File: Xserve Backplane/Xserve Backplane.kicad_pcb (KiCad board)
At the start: 4 copper layers, 100 x 100 mm, 47 parts, among them CN1 0678008025_SATA_Conn, CN2 0678008025_SATA_Conn, CN3 0678008025_SATA_Conn, J2 Conn_02x03_Odd_Even, J3 1888019-2, J4 SATA_Combo, J5 SATA_Combo, J6 SATA_Combo, Q1 Q_NMOS_DGS, Q2 Q_NMOS_DGS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

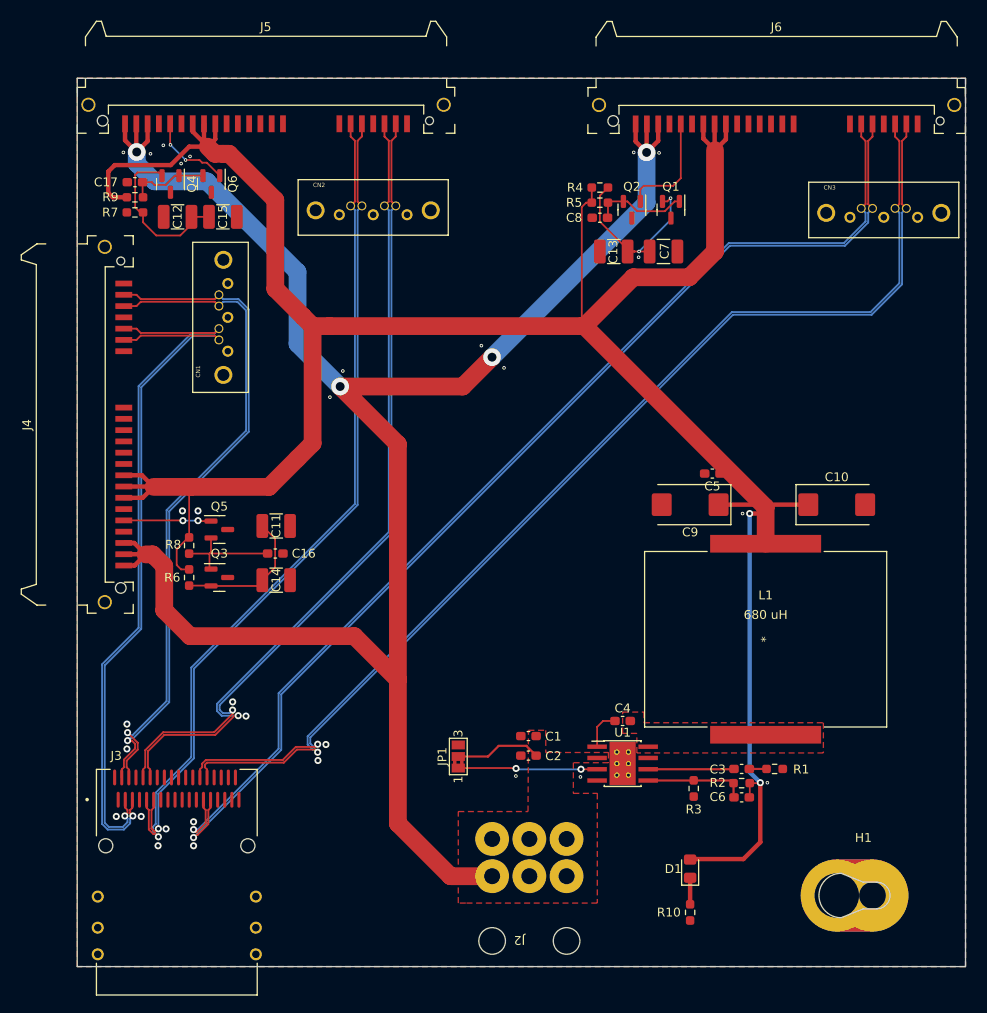
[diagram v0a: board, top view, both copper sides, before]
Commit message: "Ran DRC, changed mosfet footprint"
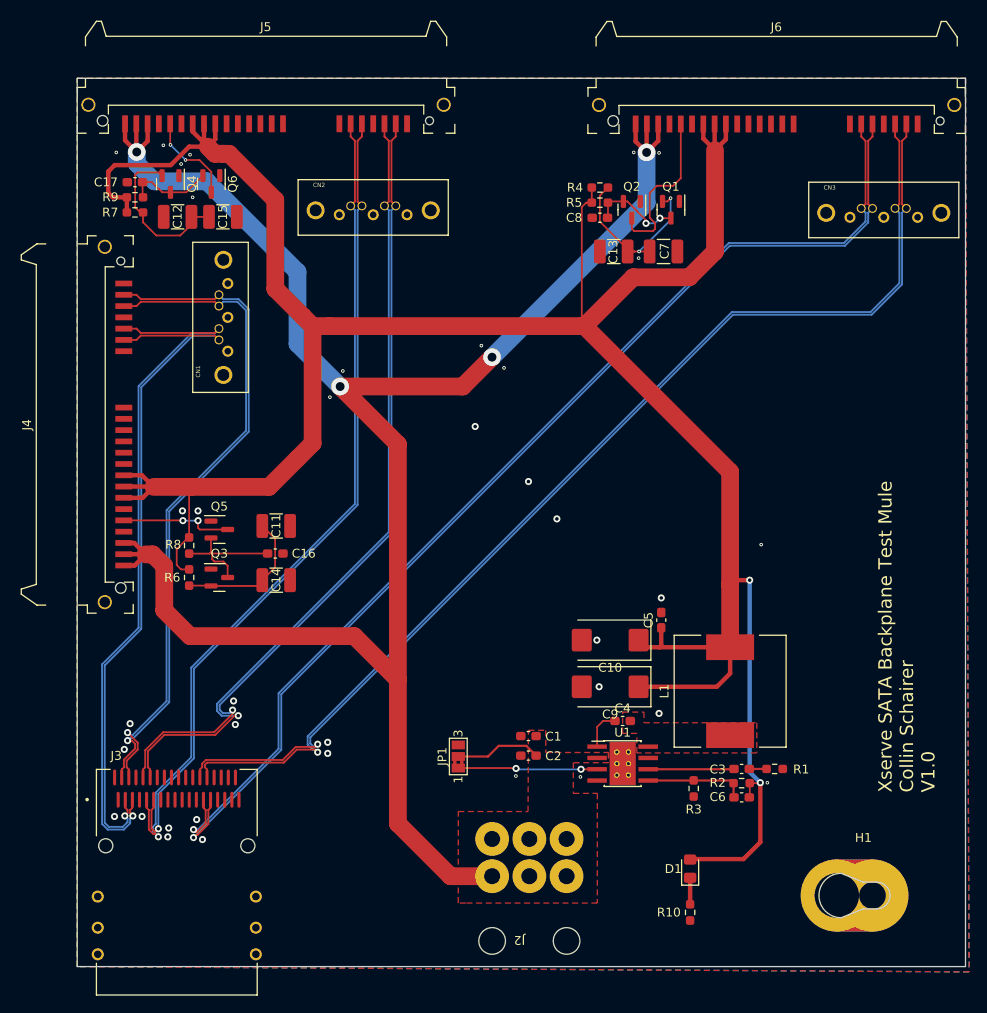
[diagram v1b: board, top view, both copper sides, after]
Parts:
- L1: value 680 uH -> 15 uH; footprint KiCADs:60B474C -> Inductor_SMD:L_12x12mm_H8mm
- moved G*** 71.4 mm to (230.0, 236.2)
- moved C10 29.7 mm to (279.0, 206.2), turned to 180 degrees
- moved C9 22.4 mm to (279.0, 211.5)
- moved C5 17.5 mm to (284.8, 204.0), turned to 90 degrees
- moved L1 7.09 mm to (292.5, 212.0)
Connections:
- C1 pad 2: GND -> Earth
- C10 pad 2: GND -> Earth
- C11 pad 2: GND -> Earth
- C12 pad 2: GND -> Earth
- C13 pad 2: GND -> Earth
- C14 pad 2: GND -> Earth
- C15 pad 2: GND -> Earth
- C16 pad 2: GND -> Earth
- C17 pad 2: GND -> Earth
- C2 pad 2: GND -> Earth
- C5 pad 2: GND -> Earth
- C7 pad 2: GND -> Earth
- C8 pad 2: GND -> Earth
- C9 pad 2: GND -> Earth
- CN1 pad GND1: GND -> Earth
- CN1 pad GND2: GND -> Earth
- CN1 pad GND3: GND -> Earth
- CN1 pad MNT1: GND -> Earth
- CN1 pad MNT2: GND -> Earth
- CN2 pad GND1: GND -> Earth
- CN2 pad GND2: GND -> Earth
- CN2 pad GND3: GND -> Earth
- CN2 pad MNT1: GND -> Earth
- CN2 pad MNT2: GND -> Earth
- CN3 pad GND1: GND -> Earth
- CN3 pad GND2: GND -> Earth
- CN3 pad GND3: GND -> Earth
- CN3 pad MNT1: GND -> Earth
- CN3 pad MNT2: GND -> Earth
- H1 pad 1: GND -> Earth
- J2 pad 4: GND -> Earth
- J2 pad 5: GND -> Earth
- J2 pad 6: GND -> Earth
- J3 pad A1: GND -> Earth
- J3 pad A12: GND -> Earth
- J3 pad A15: GND -> Earth
- J3 pad A18: GND -> Earth
- J3 pad A4: GND -> Earth
- J3 pad A7: GND -> Earth
- J3 pad B1: GND -> Earth
- J3 pad B12: GND -> Earth
- J3 pad B15: GND -> Earth
- J3 pad B18: GND -> Earth
- J3 pad B4: GND -> Earth
- J3 pad B7: GND -> Earth
- J3 pad S1: GND -> Earth
- J3 pad S2: GND -> Earth
- J3 pad S3: GND -> Earth
- J3 pad S4: GND -> Earth
- J3 pad S5: GND -> Earth
- J3 pad S6: GND -> Earth
- J4 pad P10: GND -> Earth
- J4 pad P12: GND -> Earth
- J4 pad P4: GND -> Earth
- J4 pad P5: GND -> Earth
- J4 pad P6: GND -> Earth
- J4 pad S1: GND -> Earth
- J4 pad S4: GND -> Earth
- J4 pad S7: GND -> Earth
- J5 pad P10: GND -> Earth
- J5 pad P12: GND -> Earth
- J5 pad P4: GND -> Earth
- J5 pad P5: GND -> Earth
- J5 pad P6: GND -> Earth
- J5 pad S1: GND -> Earth
- J5 pad S4: GND -> Earth
- J5 pad S7: GND -> Earth
- J6 pad P10: GND -> Earth
- J6 pad P12: GND -> Earth
- J6 pad P4: GND -> Earth
- J6 pad P5: GND -> Earth
- J6 pad P6: GND -> Earth
- J6 pad S1: GND -> Earth
- J6 pad S4: GND -> Earth
- J6 pad S7: GND -> Earth
- JP1 pad 3: GND -> Earth
- Q1 pad 1: Net-(C8-Pad1) -> Earth
- Q1 pad 3: GND -> Net-(C8-Pad1)
- Q2 pad 1: ACT_3 -> Earth
- Q2 pad 3: GND -> ACT_3
- Q3 pad 1: Net-(C16-Pad1) -> Earth
- Q3 pad 3: GND -> Net-(C16-Pad1)
- Q4 pad 1: Net-(C17-Pad1) -> Earth
- Q4 pad 3: GND -> Net-(C17-Pad1)
- Q5 pad 1: ACT_1 -> Earth
- Q5 pad 3: GND -> ACT_1
- Q6 pad 1: ACT_2 -> Earth
- Q6 pad 3: GND -> ACT_2
- R1 pad 2: GND -> Earth
- R10 pad 2: GND -> Earth
- R3 pad 2: GND -> Earth
- U1 pad 4: GND -> Earth
- U1 pad 7: GND -> Earth
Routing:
- net 5V: track 289.5 -> 309.3 mm
- net ACT_3: track 12.5 -> 18.6 mm
- net ACT_1: track 9.85 -> 12.7 mm
- net Net-(C16-Pad1): track 12.4 -> 14.6 mm
- net ACT_2: track 9.37 -> 10.5 mm
- net Net-(C17-Pad1): track 9.06 -> 9.76 mm
- net Net-(C8-Pad1): track 10.7 -> 10.4 mm, vias 0 -> 2
- net Earth: track 0.00 -> 0.25 mm, vias 0 -> 37
- net GND: vias 30 -> 0
- added copper zone on B.Cu, net Earth
- added copper zone on F.Cu, net Earth
- added copper zone on In1.Cu, net Earth
- added copper zone on In2.Cu, net Earth
- removed copper zone on B.Cu, net GND
- removed copper zone on F.Cu, net GND
- removed copper zone on In1.Cu, net GND
- removed copper zone on In2.Cu, net GND
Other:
- board text added: "Xserve SATA Backplane Test Mule Collin Schairer V1.0"

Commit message: Creatd Ampehnol SAS connector footprint and implemented in schematic. Began implementation in layout.
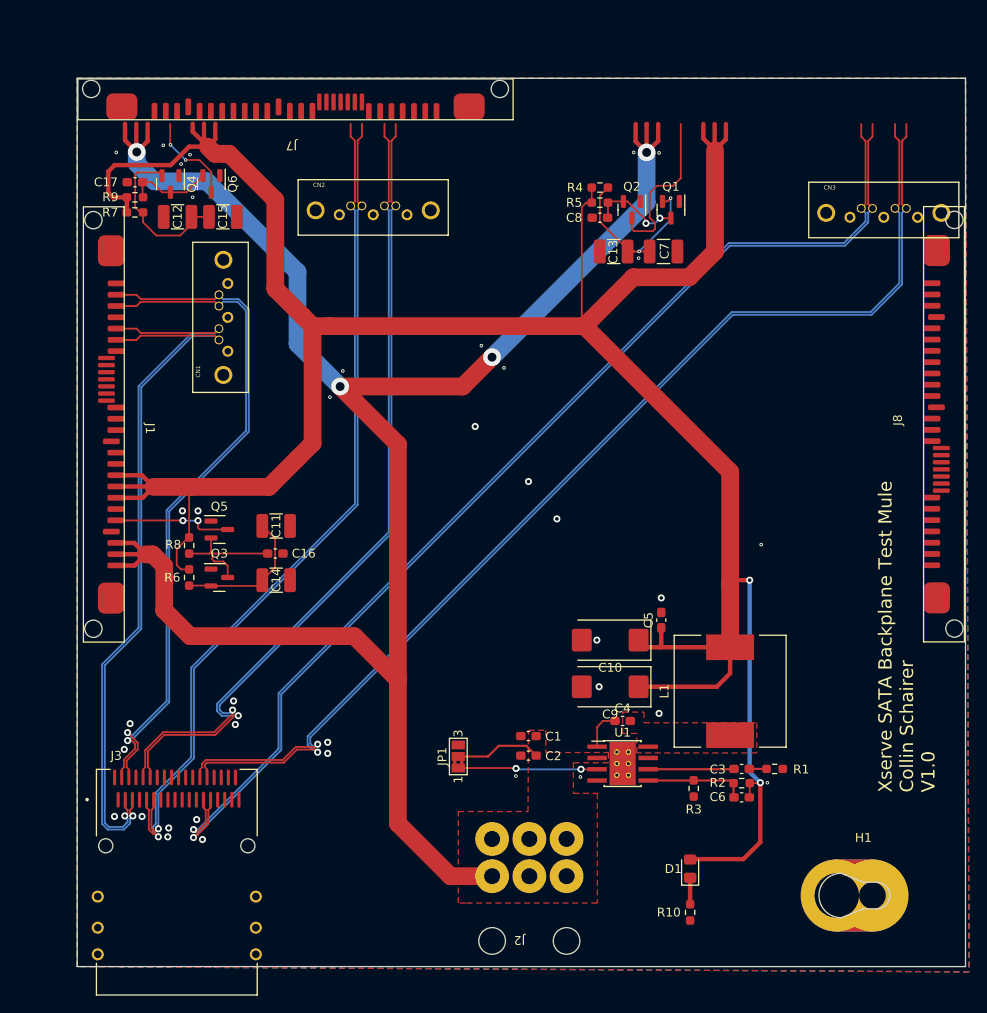
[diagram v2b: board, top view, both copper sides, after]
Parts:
- removed G***: LOGO, KiCADs:TheColonelCu
- removed J4, J5, J6: SATA_Combo, Connector_SATA_SAS:SATA_Amphenol_10029364-001LF_Horizontal
- added J1: ~, KiCADs:10124274-001TRLF, F.Cu at (220.8, 182.0)
- added J7: ~, KiCADs:10124274-001TRLF, F.Cu at (243.6, 144.2)
- added J8: ~, KiCADs:10124274-001TRLF, F.Cu at (317.8, 181.9)
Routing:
- net Earth: vias 37 -> 0
- net 3V3: vias 0 -> 37
- added copper zone on B.Cu, net 3V3
- added copper zone on F.Cu, net 3V3
- added copper zone on In1.Cu, net 3V3
- added copper zone on In2.Cu, net 3V3
- removed copper zone on B.Cu, net Earth
- removed copper zone on F.Cu, net Earth
- removed copper zone on In1.Cu, net Earth
- removed copper zone on In2.Cu, net Earth

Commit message: created SAS connector footprint and added to layout. next step is routing with new connector
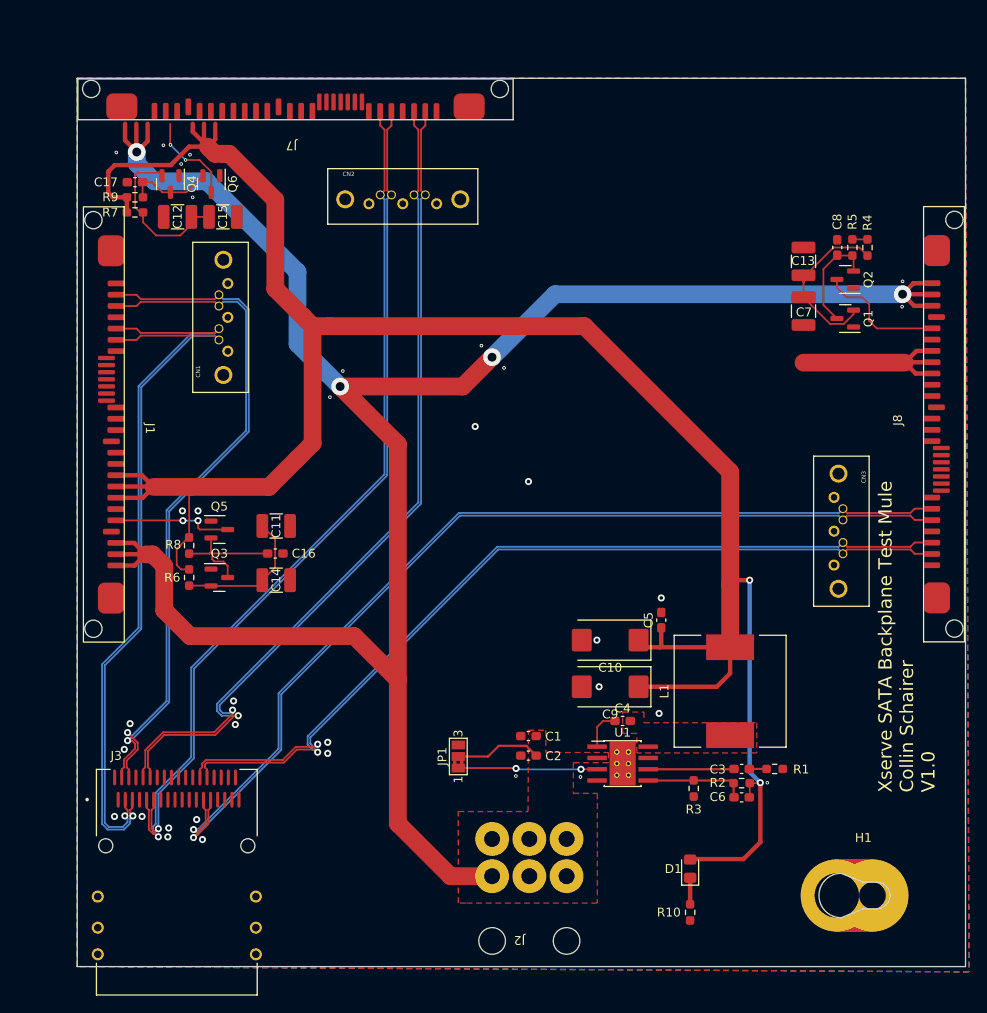
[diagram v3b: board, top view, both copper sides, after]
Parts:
- added TP1: TestPoint_Probe, KiCADs:TheColonelCu, F.Cu at (230.6, 235.4)
- moved CN3 36.2 mm to (304.7, 194.0), turned to -90 degrees
- moved R4 30.9 mm to (308.0, 162.1), turned to -90 degrees
- moved R5 28.9 mm to (306.3, 162.1), turned to -90 degrees
- moved C8 26.9 mm to (304.6, 162.1), turned to 90 degrees
- moved Q2 25.3 mm to (305.5, 165.7), turned to 180 degrees
- moved Q1 23.1 mm to (305.5, 170.1), turned to 180 degrees
- moved C13 21.4 mm to (300.8, 163.6), turned to 90 degrees
- moved C7 17.1 mm to (300.8, 169.2), turned to -90 degrees
- moved CN2 3.55 mm to (255.7, 156.6)
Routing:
- net 5V: track 309.3 -> 276.4 mm
- net A3+: track 123.8 -> 96.2 mm
- net A3-: track 123.8 -> 96.7 mm
- net 12V: track 230.0 -> 248.9 mm
- net B3-: track 125.1 -> 107.0 mm
- net B3+: track 123.9 -> 106.3 mm
- net ACT_3: track 18.6 -> 14.5 mm
- net B2+: track 95.4 -> 98.0 mm
- net A2+: track 91.5 -> 94.1 mm
- net B2-: track 93.6 -> 96.2 mm
- net A2-: track 92.2 -> 94.8 mm
- net Net-(Q1-D): track 10.4 -> 12.0 mm, vias 2 -> 0
- net Net-(Q1-G): track 20.5 -> 19.8 mm, vias 2 -> 0
- net 3V3: vias 37 -> 34
- added copper zone on B.Cu, net Earth
- added copper zone on F.Cu, net Earth
- added copper zone on In1.Cu, net Earth
- added copper zone on In2.Cu, net Earth
- removed copper zone on B.Cu, net 3V3
- removed copper zone on F.Cu, net 3V3
- removed copper zone on In1.Cu, net 3V3
- removed copper zone on In2.Cu, net 3V3

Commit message: rough pass at SAS connector layout and some DRC fixes, this board should be manufacturable.
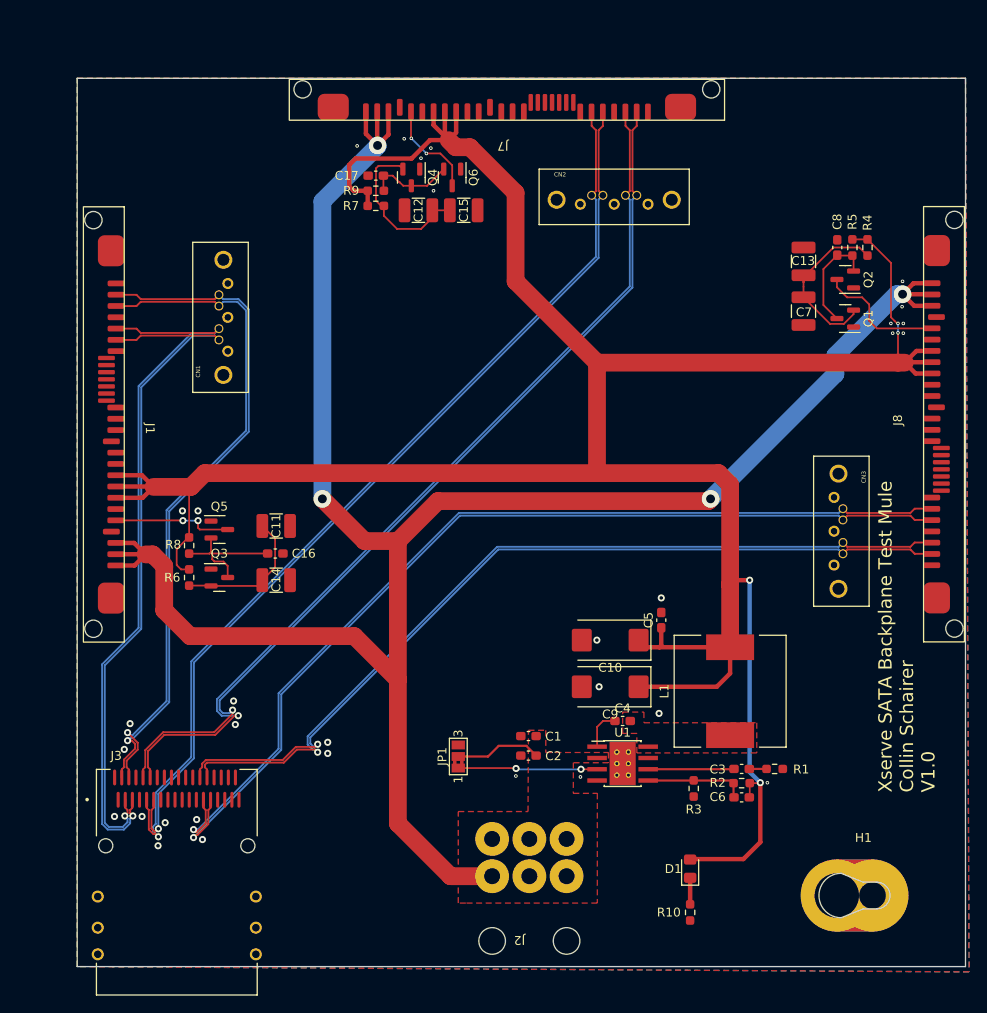
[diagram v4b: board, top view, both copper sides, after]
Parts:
- moved C12 27.1 mm to (257.4, 157.9)
- moved C17 27.1 mm to (252.6, 154.0)
- moved Q4 27.1 mm to (256.6, 154.2)
- moved R7 27.1 mm to (252.6, 157.4)
- moved R9 27.1 mm to (252.6, 155.7)
- moved C15 27.1 mm to (262.5, 157.9)
- moved Q6 27.1 mm to (261.2, 154.2)
- moved J7 23.8 mm to (267.4, 144.2)
- moved CN2 23.8 mm to (279.4, 156.7)
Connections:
- U1 pad 9: (no net) -> Earth
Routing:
- net 5V: track 276.4 -> 312.1 mm, vias 2 -> 4
- net B2-: track 96.2 -> 106.1 mm
- net A2+: track 94.1 -> 103.9 mm
- net A2-: track 94.8 -> 104.6 mm
- net B2+: track 98.0 -> 107.8 mm
- net 12V: track 248.9 -> 244.2 mm
- net Earth: vias 0 -> 32
- net 3V3: vias 34 -> 0

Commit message: misinterpreted JLC's via size capabilities. increased minimum via to 0.46 mm to comply with their requirements.
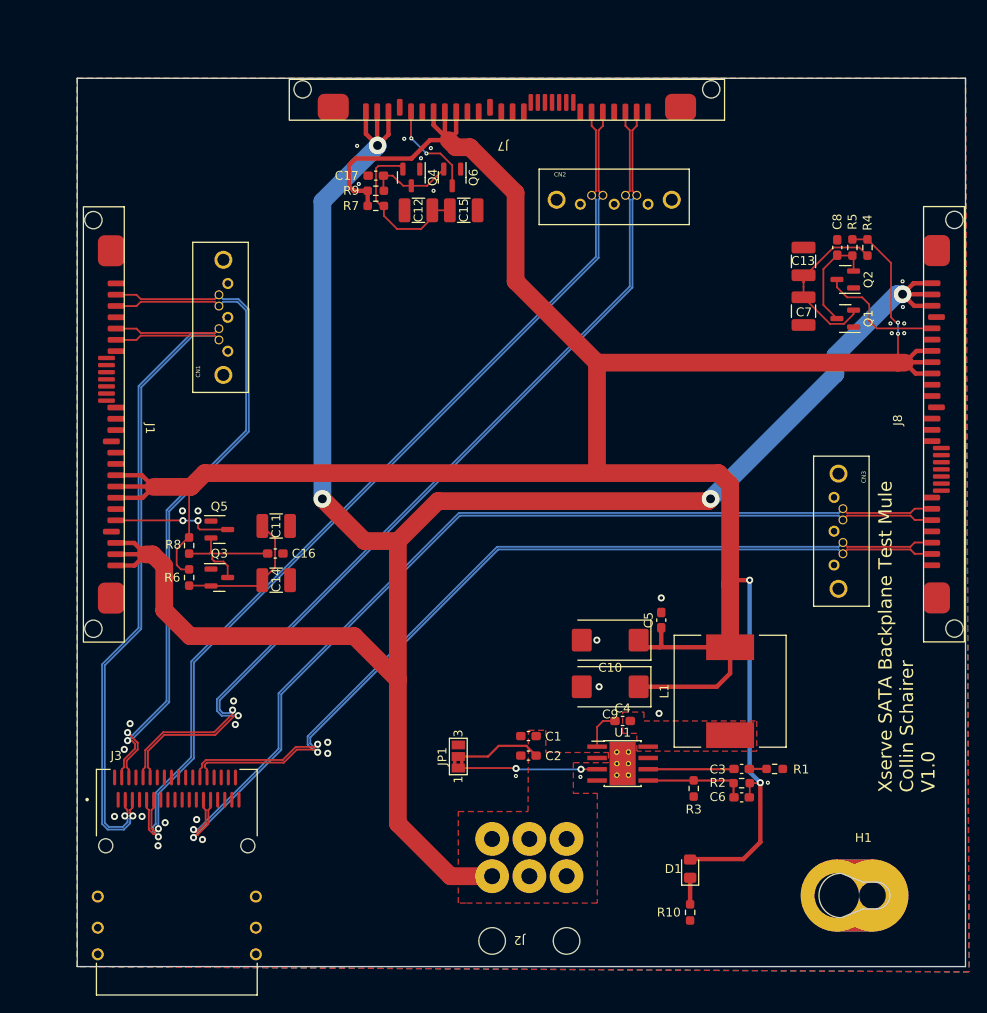
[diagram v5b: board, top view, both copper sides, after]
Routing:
- net Earth: vias 32 -> 33
